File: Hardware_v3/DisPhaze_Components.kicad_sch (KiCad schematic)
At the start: 89 parts, among them J1 SWD_Header, J2 USB_B_Micro, J3 PItch_In, J4 PD1_Amt_In, J5 PD2_Amt_In, J6 VCA_In, J7 DAC1_Out, J8 DAC2_Out, J9 Eurorack_16_pin_power, Q1 MMBT3904, Q2 MMBT3904, SW1 Octave_Switch, SW2 DAC1_RingMod_Switch, SW3 DAC2_Mix_Switch, SW4 SW_Push, U1 STM32F405RGTx, U2 TL072, U3 MCP6004, U4 LM1117-3.3, U7 LM4040DBZ-5, Y1 12MHz_18pF

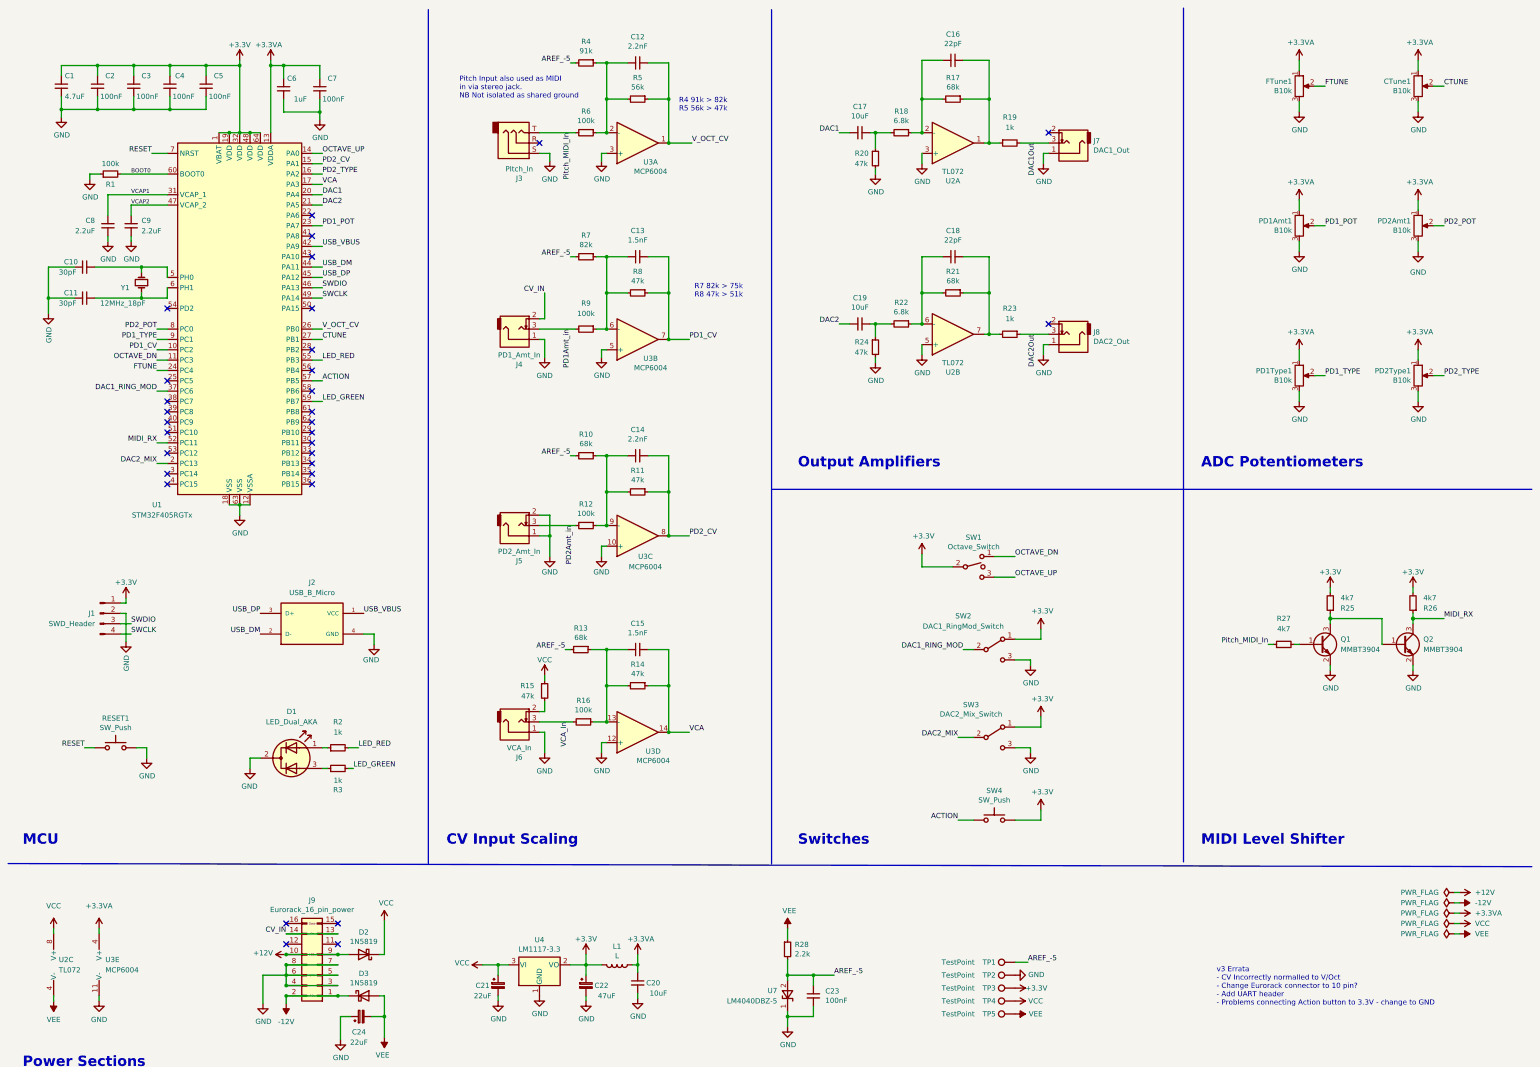
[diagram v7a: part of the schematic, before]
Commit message: Clean up of Disphaze v2 firmware
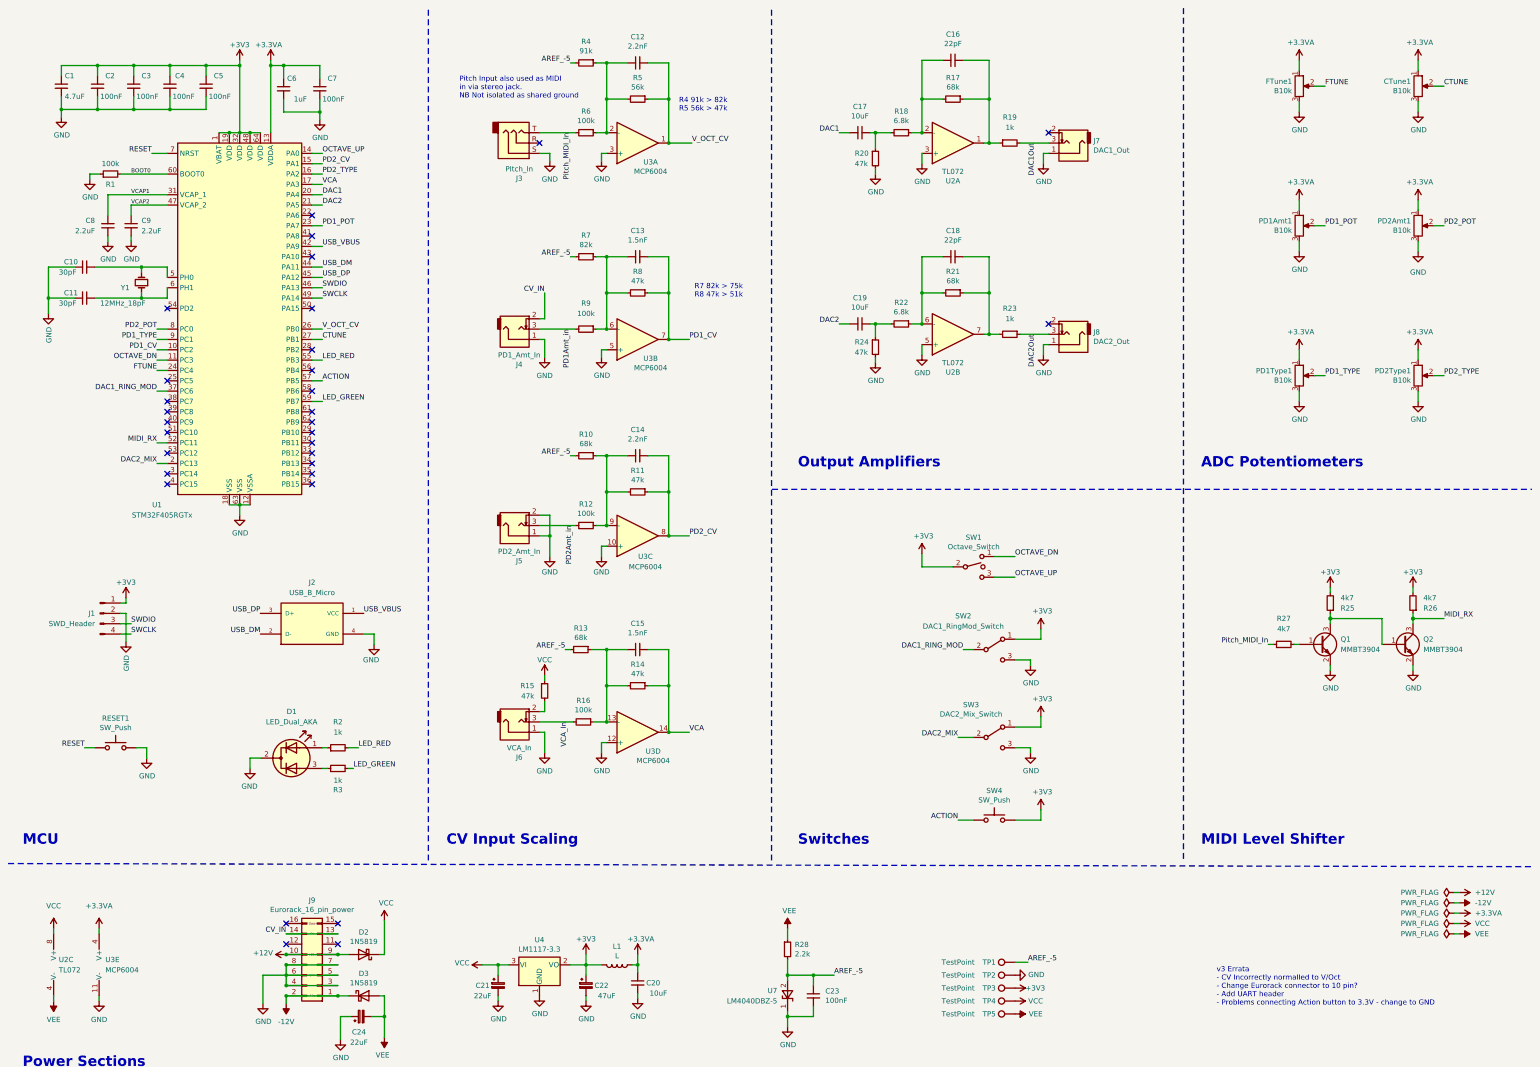
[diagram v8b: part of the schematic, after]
